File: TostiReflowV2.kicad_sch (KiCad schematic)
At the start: 28 parts, among them IC1 CP2102C-A01-GQFN24, J1 USB-C USB2.0 14Pin, Q1 BC817-40, Q2 BC817-40, SW1 EN, SW2 BOOT, U1 ESP32-S3-WROOM-1-N8R2, U5 AMS1117-3.3

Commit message: Cont.
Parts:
- added C12, C13, C5, C6: 10uF (25V/20%), symbol Device:C
- added C14, C7: 0.1uF (50V/10%), Capacitor_SMD:C_0603_1608Metric, symbol Device:C
- added J2: To Resistor, Connector_PinSocket_2.54mm:PinSocket_1x02_P2.54mm_Vertical, symbol Connector:Conn_01x02_Socket
- added J3: To Thermistor, Connector_PinSocket_2.54mm:PinSocket_1x02_P2.54mm_Vertical, symbol Connector:Conn_01x02_Socket
- added J4: VIN, Connector_PinSocket_2.54mm:PinSocket_1x02_P2.54mm_Vertical, symbol Connector:Conn_01x02_Socket
- added J5: To Relay, symbol Connector:Conn_01x02_Socket
- added J6: SPI Header, Connector_PinSocket_2.54mm:PinSocket_1x06_P2.54mm_Vertical, symbol Connector:Conn_01x06_Socket
- added Q3: NMOS, symbol Simulation_SPICE:NMOS
- added R9: 10K (1%), symbol Device:R_Small
- R4: value 22k1(1%) -> 22K1(1%)
- renumbered C13 to C10, C14 to C11, C12 to C8, C11 to C9
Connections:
- net +3V3: now also U1.2 (3V3), C13.1, C14.1, C6.2, C7.2, J2.2 (Pin_2), J6.2 (Pin_2), R9.1
- net +5V: no longer D1.1 (K), R1.2, R2.2
- net ESP32RXD: now also U1.36 (RXD0)
- net ESP32TXD: now also U1.37 (TXD0)
- net ESP32_EN: now also U1.3 (EN), C12.1, R9.2
- net ESP32_IO0: now also U1.27 (IO0)
- net GND: now also U1.1 (GND), U1.40 (GND), U1.41 (GND), C12.2, C13.2, C14.2, C5.1, C6.1, C7.1, J3.1 (Pin_1), J5.1 (Pin_1), J6.1 (Pin_1), Q3.3 (S)
- net VBUS: now also R1.2, R2.2
- net GPIO17: now reaches U1.10 (IO17)
- net GPIO18: now reaches U1.11 (IO18)
- net GPIO8_SDA: now reaches U1.12 (IO8)
- net ESP_D-: now reaches U1.13 (USB_D-)
- net ESP_D+: now reaches U1.14 (USB_D+)
- net GPIO3: now reaches U1.15 (IO3)
- net GPIO46: now reaches U1.16 (IO46)
- net GPIO9_SCL: now reaches U1.17 (IO9)
- net SPI_SS: now reaches U1.18 (IO10)
- net SPI_SS: now also J6.3 (Pin_3)
- net SPI_MOSI: now reaches U1.19 (IO11)
- net SPI_MOSI: now also J6.4 (Pin_4)
- net SPI_SCLK: now reaches U1.20 (IO12)
- net SPI_SCLK: now also J6.5 (Pin_5)
- net SPI_MISO: now reaches U1.21 (IO13)
- net SPI_MISO: now also J6.6 (Pin_6)
- net GPIO14: now reaches U1.22 (IO14)
- net GPIO21: now reaches U1.23 (IO21)
- net GPIO47: now reaches U1.24 (IO47)
- net GPIO48: now reaches U1.25 (IO48)
- net GPIO45: now reaches U1.26 (IO45)
- net GPIO35: now reaches U1.28 (IO35)
- net GPIO36: now reaches U1.29 (IO36)
- net GPIO37: now reaches U1.30 (IO37)
- net GPIO38: now reaches U1.31 (IO38)
- net GPIO39: now reaches U1.32 (IO39)
- net GPIO40: now reaches U1.33 (IO40)
- net GPIO41: now reaches U1.34 (IO41)
- net GPIO42: now reaches U1.35 (IO42)
- net GPIO2_RELAY: now reaches U1.38 (IO2)
- net GPIO2_RELAY: now also J5.2 (Pin_2)
- net GPIO1_TEMPSENS: now reaches U1.39 (IO1)
- net GPIO1_TEMPSENS: now also C5.2, J2.1 (Pin_1), J3.2 (Pin_2)
- net GPIO4: now reaches U1.4 (IO4)
- net GPIO5: now reaches U1.5 (IO5)
- net GPIO6: now reaches U1.6 (IO6)
- net GPIO7: now reaches U1.7 (IO7)
- net GPIO15: now reaches U1.8 (IO15)
- net GPIO16: now reaches U1.9 (IO16)
- new net: J4.2 (Pin_2), Q3.1 (D)
- new net VCC: D1.1 (K), J4.1 (Pin_1), Q3.2 (G)
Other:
- note added: "Automatic Programming Circuit"
- note added: "BOOT Button"
- note added: "EN Button"
- note added: "ESP32-S3-WROOM-1"
- note added: "External Power"
- note added: "Power Converter"
- note added: "Relay control"
- note added: "SPI Screen Header"
- note added: "Temperature Sensing"
- note added: "USB-C"
- note added: "USB-UART bridge"
- moved on the sheet: C1, C10, C11, C2, C3, C4, C8, C9, D1, D2, D3, D4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

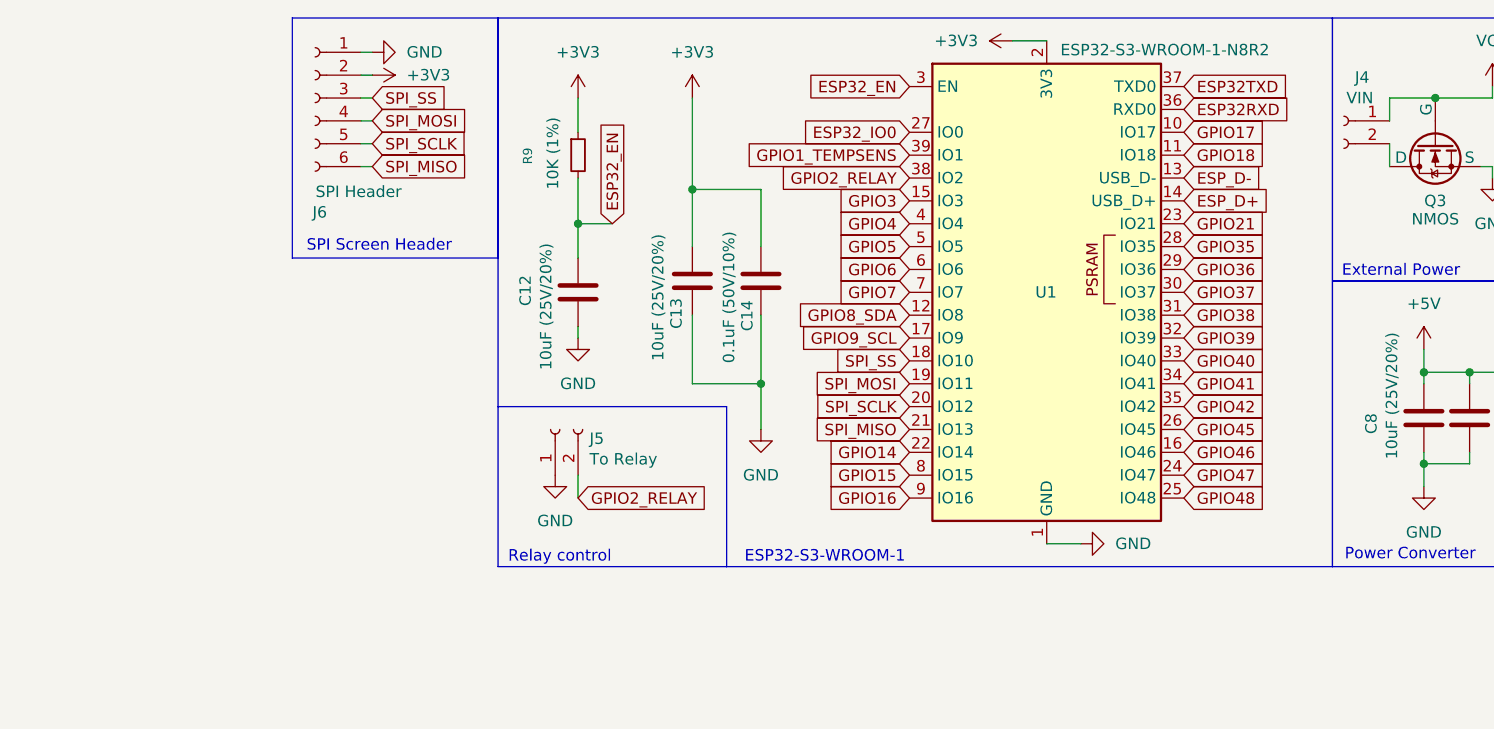
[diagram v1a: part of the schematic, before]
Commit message: added all headers
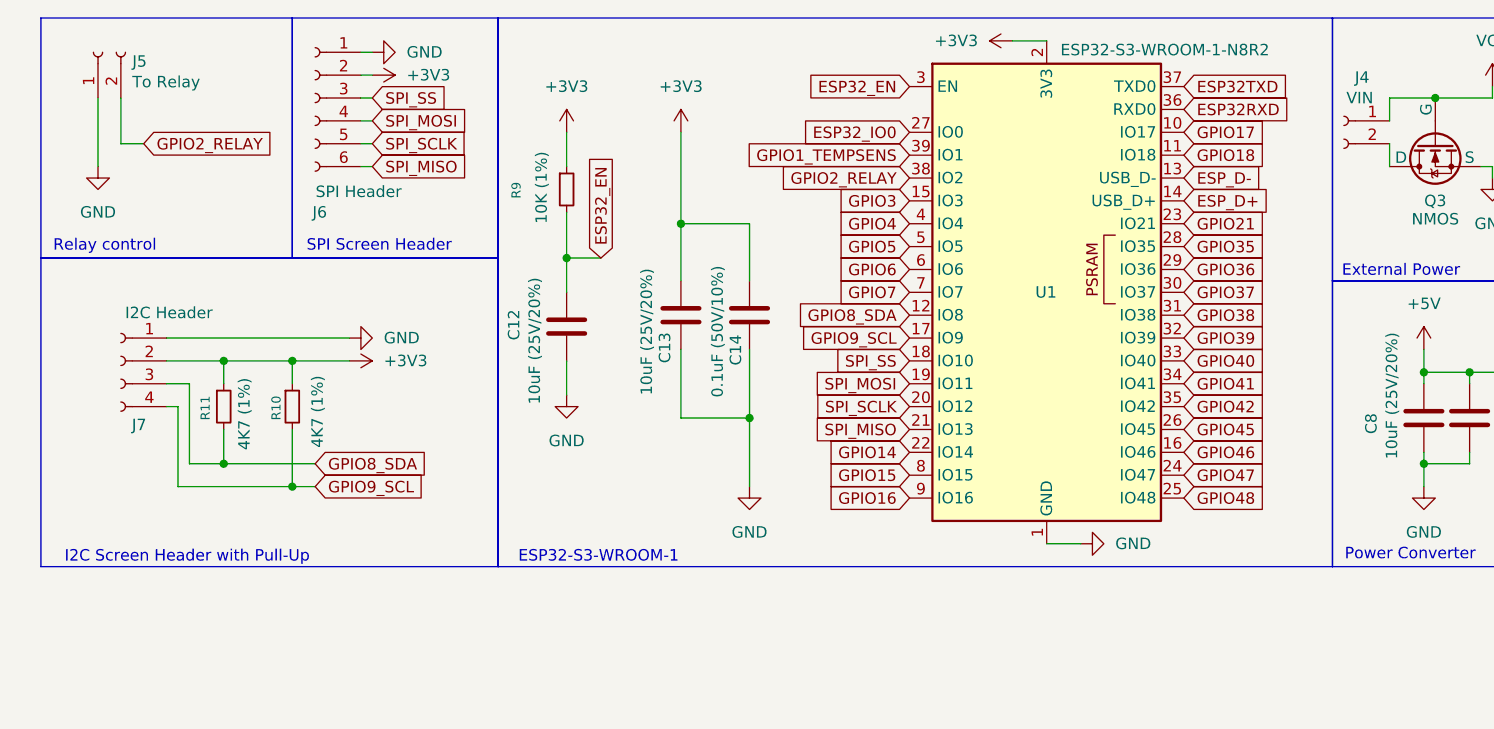
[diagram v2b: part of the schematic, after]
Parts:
- added J7: I2C Header, Connector_PinHeader_2.54mm:PinHeader_1x04_P2.54mm_Vertical, symbol Connector:Conn_01x04_Socket
- added R10, R11: 4K7 (1%), Resistor_SMD:R_0603_1608Metric, symbol Device:R_Small
- C12, C13, C5, C6: footprint (none) -> Capacitor_SMD:C_0603_1608Metric
- J5: footprint (none) -> Connector_PinSocket_2.54mm:PinSocket_1x02_P2.54mm_Vertical
- Q3: footprint (none) -> Package_TO_SOT_SMD:SOT-23
- R9: footprint (none) -> Resistor_SMD:R_0603_1608Metric
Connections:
- net +3V3: now also J7.2 (Pin_2), R10.1, R11.1
- net GND: now also J7.1 (Pin_1)
- net GPIO8_SDA: now also J7.3 (Pin_3), R11.2
- net GPIO9_SCL: now also J7.4 (Pin_4), R10.2
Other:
- note added: "I2C Screen Header with Pull-Up"
- moved on the sheet: C12, C13, C14, J5, R9
